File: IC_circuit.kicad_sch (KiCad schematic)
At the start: 18 parts, among them IC1 NRF54L10-QFAA-R, Y1 32MHz

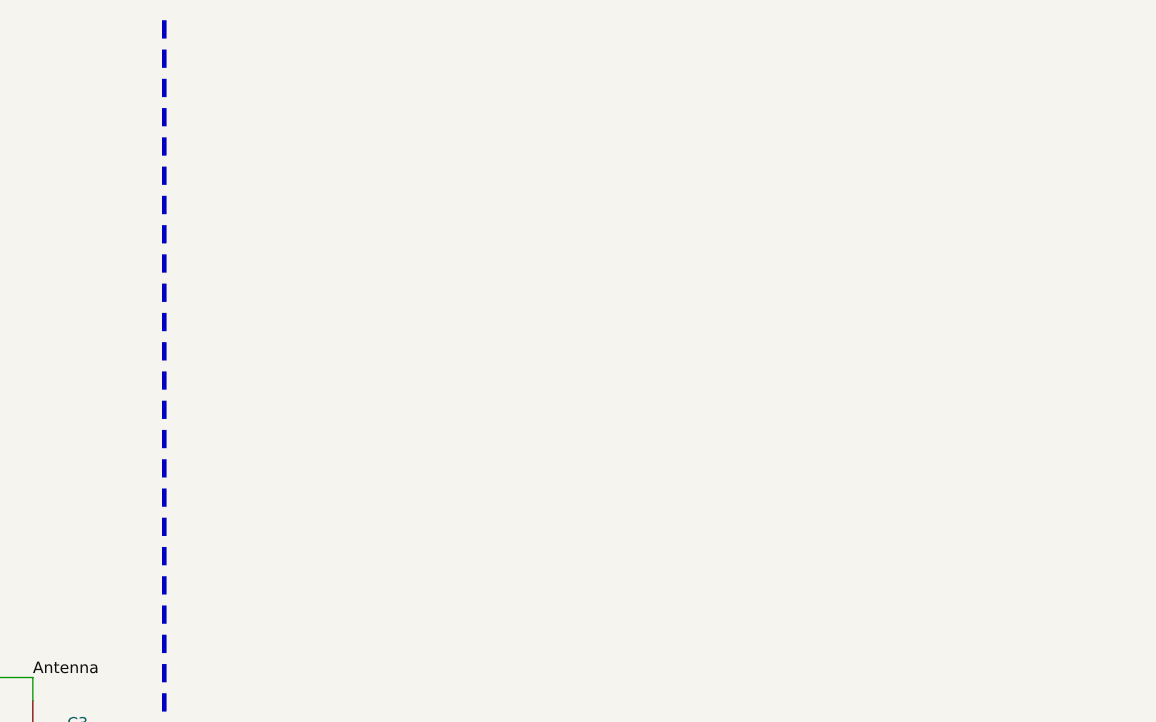
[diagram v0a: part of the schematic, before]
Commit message: Updated antenna and began work on touch circuitry
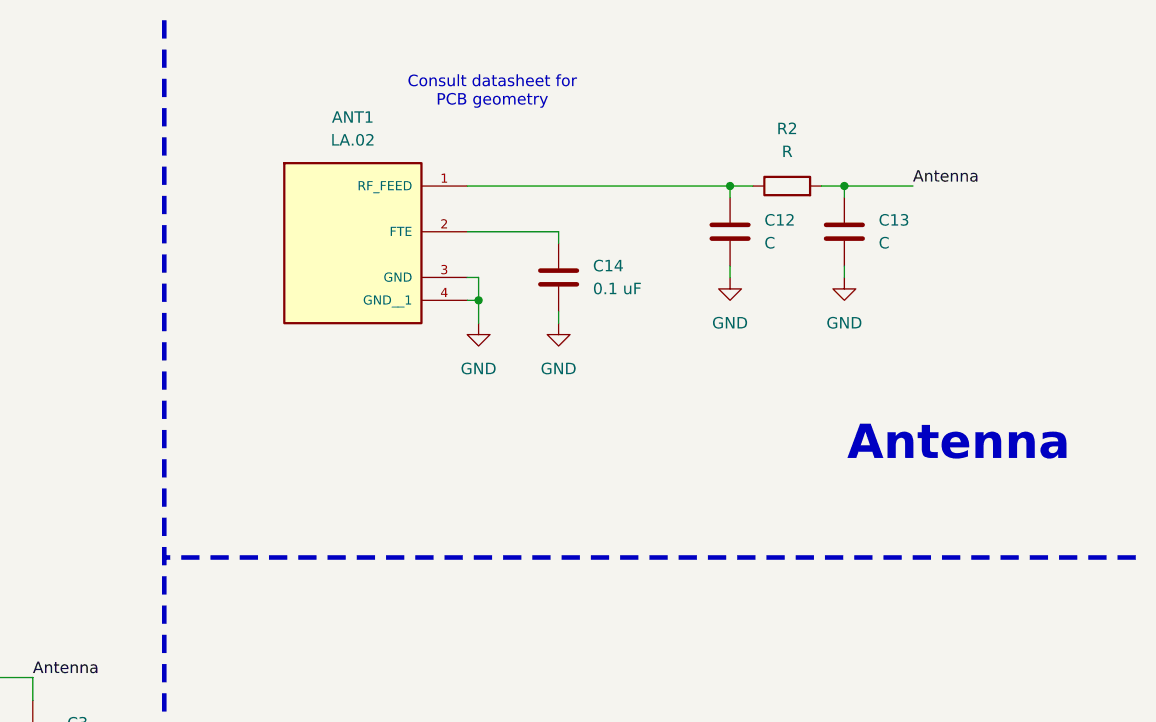
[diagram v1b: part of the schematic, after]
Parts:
- added ANT1: LA.02, LA.02:XCVR_LA.02, symbol LA.02:LA.02
- added C12, C13: C, symbol Device:C
- added C14: 0.1 uF, symbol Device:C
- added R2: R, symbol Device:R
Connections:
- net Antenna: now also C13.1, R2.2
- net GND: now also ANT1.3 (GND), ANT1.4 (GND__1), C12.2, C13.2, C14.2
- new net: ANT1.1 (RF_FEED), C12.1, R2.1
- new net: ANT1.2 (FTE), C14.1
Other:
- note added: "Antenna"
- note added: "Consult datasheet for PCB geometry"
